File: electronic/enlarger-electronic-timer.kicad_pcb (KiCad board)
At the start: 2 copper layers, 1 part

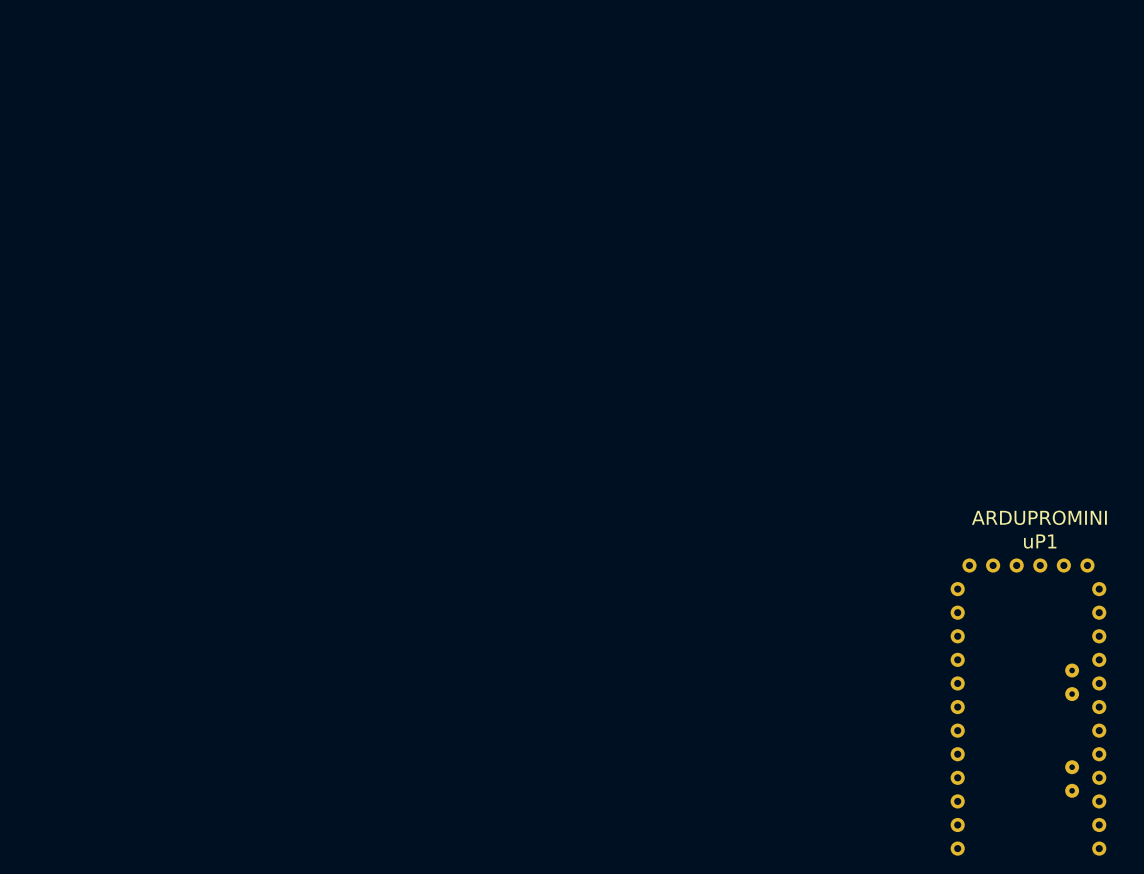
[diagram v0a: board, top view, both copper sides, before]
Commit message: Added buttons, USB. placed components on PCB
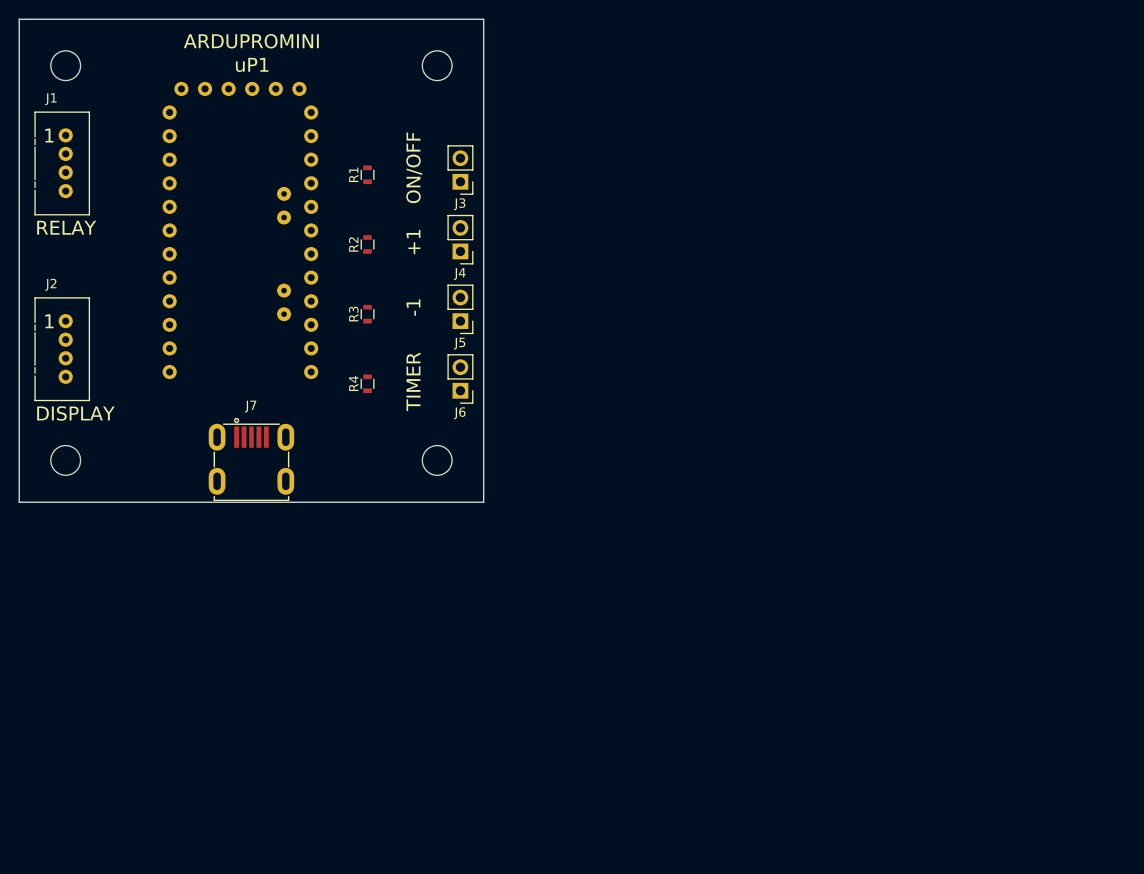
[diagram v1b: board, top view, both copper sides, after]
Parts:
- added J1: RELAY, Connectors:Grove_1x04, F.Cu at (55.0, 62.5)
- added J2: DIGIT, Connectors:Grove_1x04, F.Cu at (55.0, 82.5)
- added J3: FORCE, Pin_Headers:Pin_Header_Straight_1x02_Pitch2.54mm, F.Cu at (97.5, 67.5)
- added J4: INCREASE, Pin_Headers:Pin_Header_Straight_1x02_Pitch2.54mm, F.Cu at (97.5, 75.0)
- added J5: DECREASE, Pin_Headers:Pin_Header_Straight_1x02_Pitch2.54mm, F.Cu at (97.5, 82.5)
- added J6: TIMER, Pin_Headers:Pin_Header_Straight_1x02_Pitch2.54mm, F.Cu at (97.5, 90.0)
- added J7: USB_OTG, lib_fp:ST-USB-013A, F.Cu at (75.0, 95.0)
- added R1: 10K, Resistors_SMD:R_0603, F.Cu at (87.5, 66.8)
- added R2: 10K, Resistors_SMD:R_0603, F.Cu at (87.5, 74.2)
- added R3: 10K, Resistors_SMD:R_0603, F.Cu at (87.5, 81.8)
- added R4: 10K, Resistors_SMD:R_0603, F.Cu at (87.5, 89.2)
- added REF**: MountingHole_3.2mm_M3, Mounting_Holes:MountingHole_3.2mm_M3, F.Cu at (55.0, 97.5)
- added REF**: MountingHole_3.2mm_M3, Mounting_Holes:MountingHole_3.2mm_M3, F.Cu at (55.0, 55.0)
- added REF**: MountingHole_3.2mm_M3, Mounting_Holes:MountingHole_3.2mm_M3, F.Cu at (95.0, 55.0)
- added REF**: MountingHole_3.2mm_M3, Mounting_Holes:MountingHole_3.2mm_M3, F.Cu at (95.0, 97.5)
- moved uP1 99.2 mm to (63.6, 53.7)
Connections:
- uP1 pad 10: Net-(uP1-Pad10) -> GND
- uP1 pad 13: Net-(uP1-Pad13) -> GROVE_RELAY_D0
- uP1 pad 14: Net-(uP1-Pad14) -> GROVE_DIGIT_CLK
- uP1 pad 15: Net-(uP1-Pad15) -> GROVE_DIGIT_DIO
- uP1 pad 22: Net-(uP1-Pad22) -> VCC
- uP1 pad 27: Net-(uP1-Pad27) -> FORCE_INPUT
- uP1 pad 28: Net-(uP1-Pad28) -> INCREASE_INPUT
- uP1 pad 29: Net-(uP1-Pad29) -> DECREASE_INPUT
- uP1 pad 30: Net-(uP1-Pad30) -> TIMER_INPUT
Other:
- board outline added: 50 x 52 mm
- board text added: "+1"
- board text added: "-1"
- board text added: "DISPLAY"
- board text added: "ON/OFF"
- board text added: "RELAY"
- board text added: "TIMER"

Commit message: Wired pcb
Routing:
- net FORCE_INPUT: track 0.00 -> 29.1 mm, vias 0 -> 4
- net INCREASE_INPUT: track 0.00 -> 24.1 mm, vias 0 -> 2
- net GROVE_RELAY_D0: track 0.00 -> 23.8 mm, vias 0 -> 2
- net DECREASE_INPUT: track 0.00 -> 19.1 mm, vias 0 -> 2
- net TIMER_INPUT: track 0.00 -> 18.1 mm, vias 0 -> 2
- net GROVE_DIGIT_CLK: track 0.00 -> 15.8 mm, vias 0 -> 2
- net GROVE_DIGIT_DIO: track 0.00 -> 15.2 mm, vias 0 -> 2
- net VCC: track 0.00 -> 2.54 mm, vias 0 -> 1
- net GND: track 0.00 -> 2.54 mm, vias 0 -> 1
- added copper zone on B.Cu, net GND
- added copper zone on F.Cu, net VCC
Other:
- net class DATA added: clearance 0.2, trace_width 0.5, via_dia 0.6, via_drill 0.4
- net class POWER added: clearance 0.2, trace_width 0.5, via_dia 0.6, via_drill 0.4
